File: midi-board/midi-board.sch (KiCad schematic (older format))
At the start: 22 parts, among them J1 MIDI OUT, J2 MIDI IN, J3 UART Header, U1 74LVC1G06, U2 74LVC1G17, U3 TLP185(SE

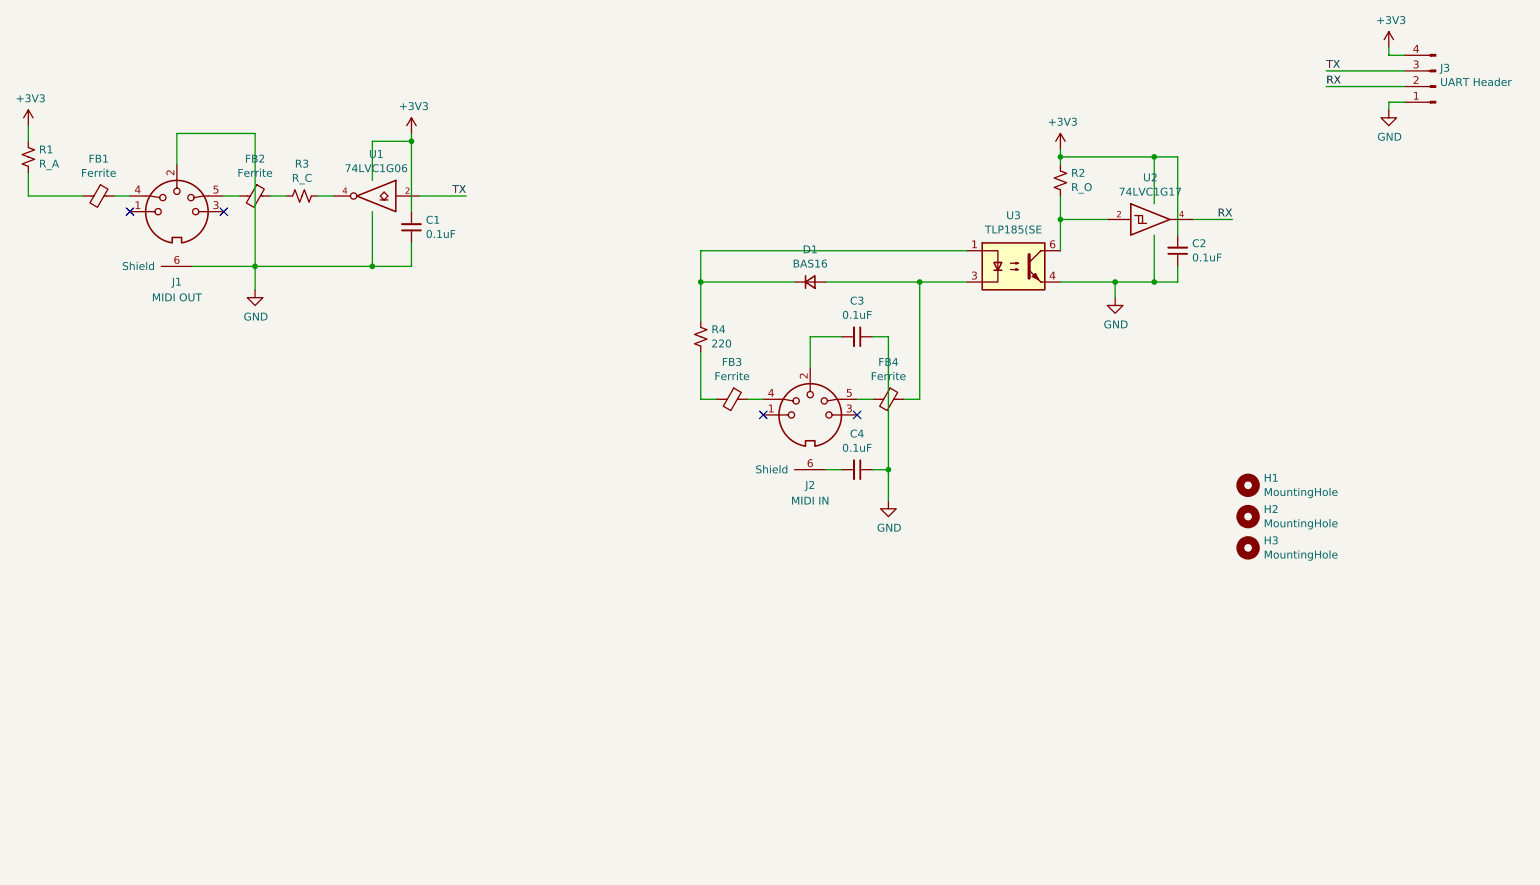
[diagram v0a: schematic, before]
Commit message: Converted MIDI board to I2C
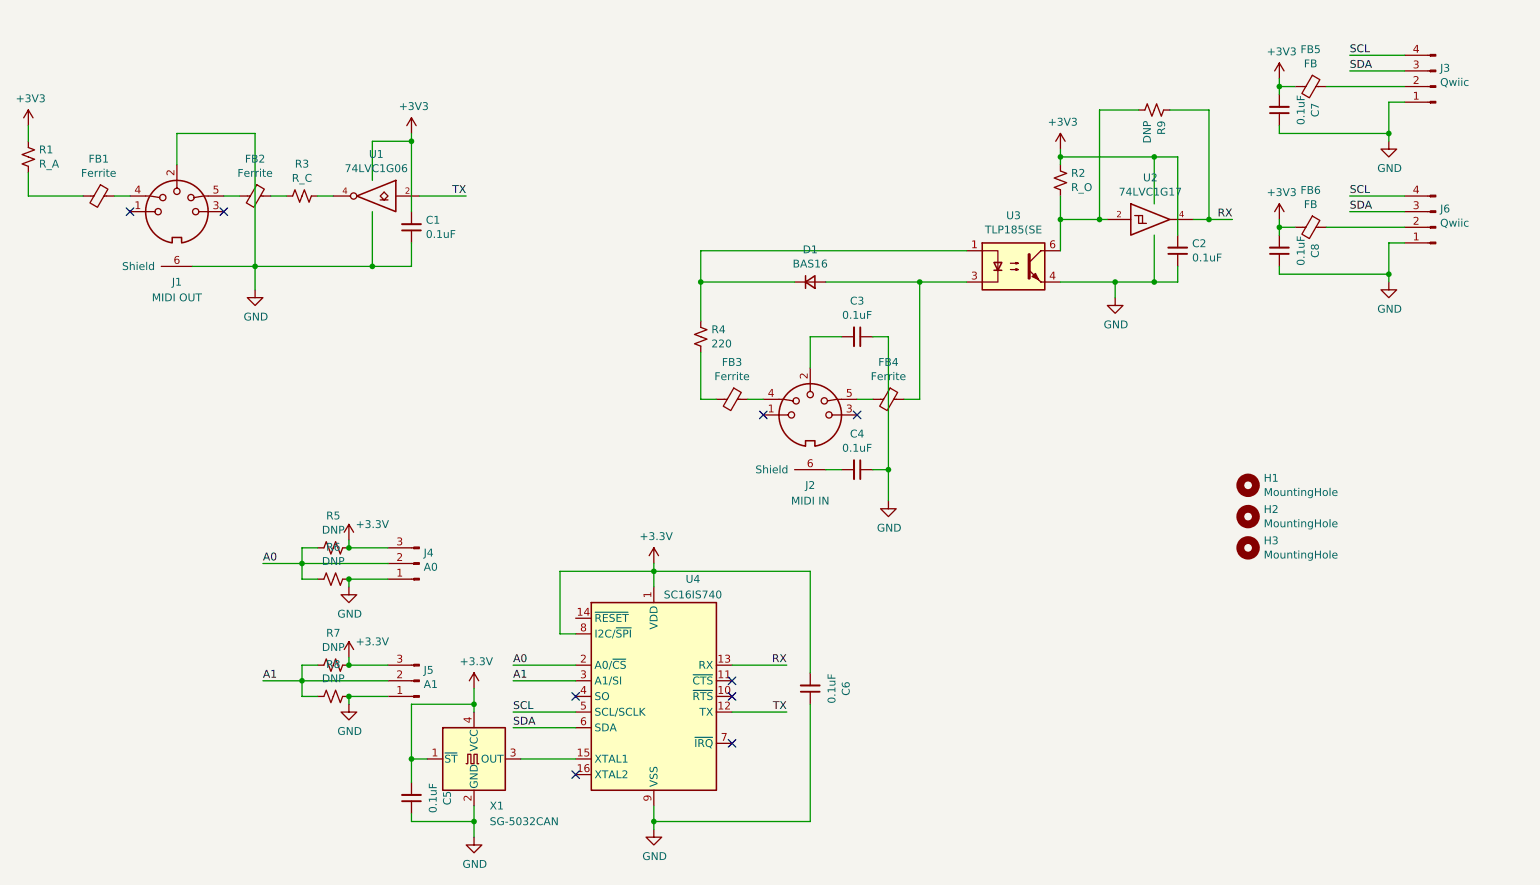
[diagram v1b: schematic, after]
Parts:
- added C5, C6, C7, C8: 0.1uF, Capacitors_SMD:C_0805_HandSoldering, symbol Device:C_Small
- added FB5, FB6: FB, Inductors_SMD:L_0805_HandSoldering, symbol Device:Ferrite_Bead_Small
- added J4: A0, Pin_Headers:Pin_Header_Straight_1x03_Pitch2.54mm, symbol Connector:Conn_01x03_Male
- added J5: A1, Pin_Headers:Pin_Header_Straight_1x03_Pitch2.54mm, symbol Connector:Conn_01x03_Male
- added J6: Qwiic, Connectors_JST:JST_SH_SM04B-SRSS-TB_04x1.00mm_Angled, symbol Connector:Conn_01x04_Male
- added R5, R6, R7, R8, R9: DNP, Resistors_SMD:R_0805_HandSoldering, symbol Device:R_Small_US
- added U4: SC16IS740, Housings_SSOP:TSSOP-16_4.4x5mm_Pitch0.65mm, symbol Interface_UART:SC16IS740
- added X1: SG-5032CAN, Oscillators:Oscillator_SMD_SeikoEpson_SG8002CE-4pin_3.2x2.5mm_HandSoldering, symbol Oscillator:SG-5032CAN
- J3: value UART Header -> Qwiic; footprint Pin_Headers:Pin_Header_Angled_1x04_Pitch2.54mm -> Connectors_JST:JST_SH_SM04B-SRSS-TB_04x1.00mm_Angled
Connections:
- net +3V3: now also C5.2, C6.2, C7.2, C8.2, FB5.2, FB6.2, J4.3 (Pin_3), J5.3 (Pin_3), R5.1, R7.1, U4.1 (VDD), U4.8 (I2C/~SPI), X1.1 (~ST), X1.4 (VCC); no longer J3.4 (Pin_4)
- net GND: now also C5.1, C6.1, C7.1, C8.1, J4.1 (Pin_1), J5.1 (Pin_1), J6.1 (Pin_1), R6.1, R8.1, U4.9 (VSS), X1.2 (GND)
- net RX: now also R9.1, U4.13 (RX); no longer J3.2 (Pin_2)
- net TX: now also U4.12 (TX); no longer J3.3 (Pin_3)
- net at R2.2, U2.2, U3.6: now also R9.2
- new net: FB5.1, J3.2 (Pin_2)
- new net: U4.15 (XTAL1), X1.3 (OUT)
- new net: FB6.1, J6.2 (Pin_2)
- new net A0: J4.2 (Pin_2), R5.2, R6.2, U4.2 (A0/~CS)
- new net A1: J5.2 (Pin_2), R7.2, R8.2, U4.3 (A1/SI)
- new net SCL: J3.4 (Pin_4), J6.4 (Pin_4), U4.5 (SCL/SCLK)
- new net SDA: J3.3 (Pin_3), J6.3 (Pin_3), U4.6 (SDA)
- no-connect marks 4 -> 9

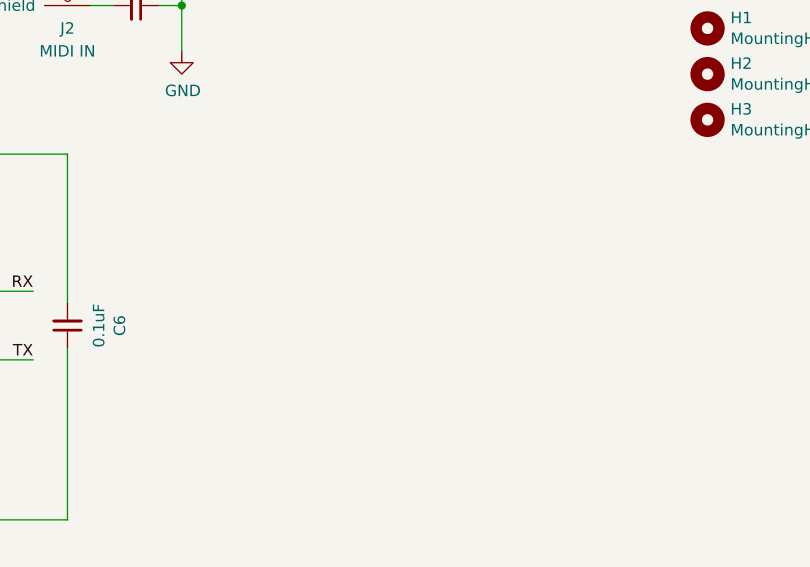
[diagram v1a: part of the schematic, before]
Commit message: Include a debug header for the TX/RX lines in their TTL state.
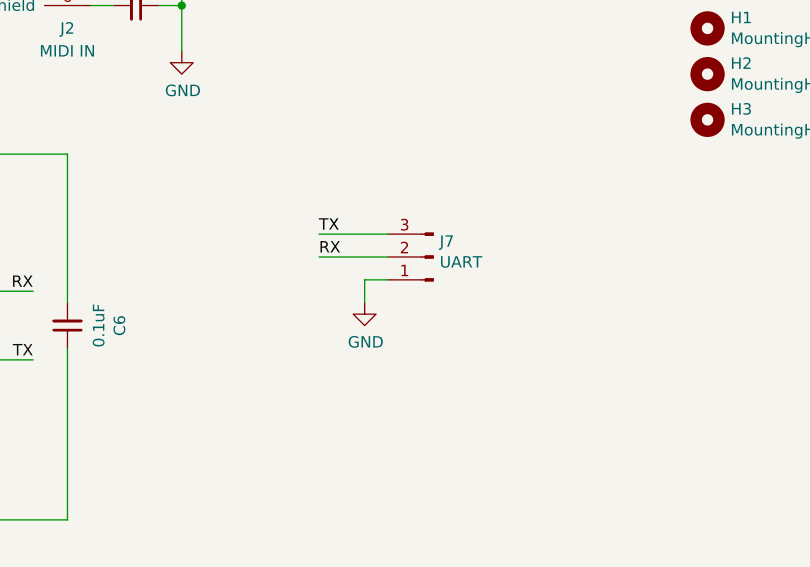
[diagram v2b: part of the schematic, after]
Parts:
- added J7: UART, Pin_Headers:Pin_Header_Straight_1x03_Pitch2.54mm, symbol Connector:Conn_01x03_Male
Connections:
- net GND: now also J7.1 (Pin_1)
- net RX: now also J7.2 (Pin_2)
- net TX: now also J7.3 (Pin_3)
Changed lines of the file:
@@
 Wire Wire Line
 	8750 2100 8900 2100
+$Comp
+L Connector:Conn_01x03_Male J7
+U 1 1 5FFC58E3
+P 7800 4800
+F 0 "J7" H 7772 4732 50  0000 R CNN
+F 1 "UART" H 7772 4823 50  0000 R CNN
+F 2 "Pin_Headers:Pin_Header_Straight_1x03_Pitch2.54mm" H 7800 4800 50  0001 C CNN
+F 3 "~" H 7800 4800 50  0001 C CNN
+	1    7800 4800
+	-1   0    0    1
+$EndComp
+Wire Wire Line
+	7600 4900 7500 4900
+Wire Wire Line
+	7500 4900 7500 5000
+$Comp
+L power:GND #PWR0119
+U 1 1 5FFCB599
+P 7500 5000
+F 0 "#PWR0119" H 7500 4750 50  0001 C CNN
+F 1 "GND" H 7505 4827 50  0000 C CNN
+F 2 "" H 7500 5000 50  0001 C CNN
+F 3 "" H 7500 5000 50  0001 C CNN
+	1    7500 5000
+	1    0    0    -1
+$EndComp
+Wire Wire Line
+	7600 4800 7300 4800
+Wire Wire Line
+	7600 4700 7300 4700
+Text Label 7300 4700 0    50   ~ 0
+TX
+Text Label 7300 4800 0    50   ~ 0
+RX
 $EndSCHEMATC

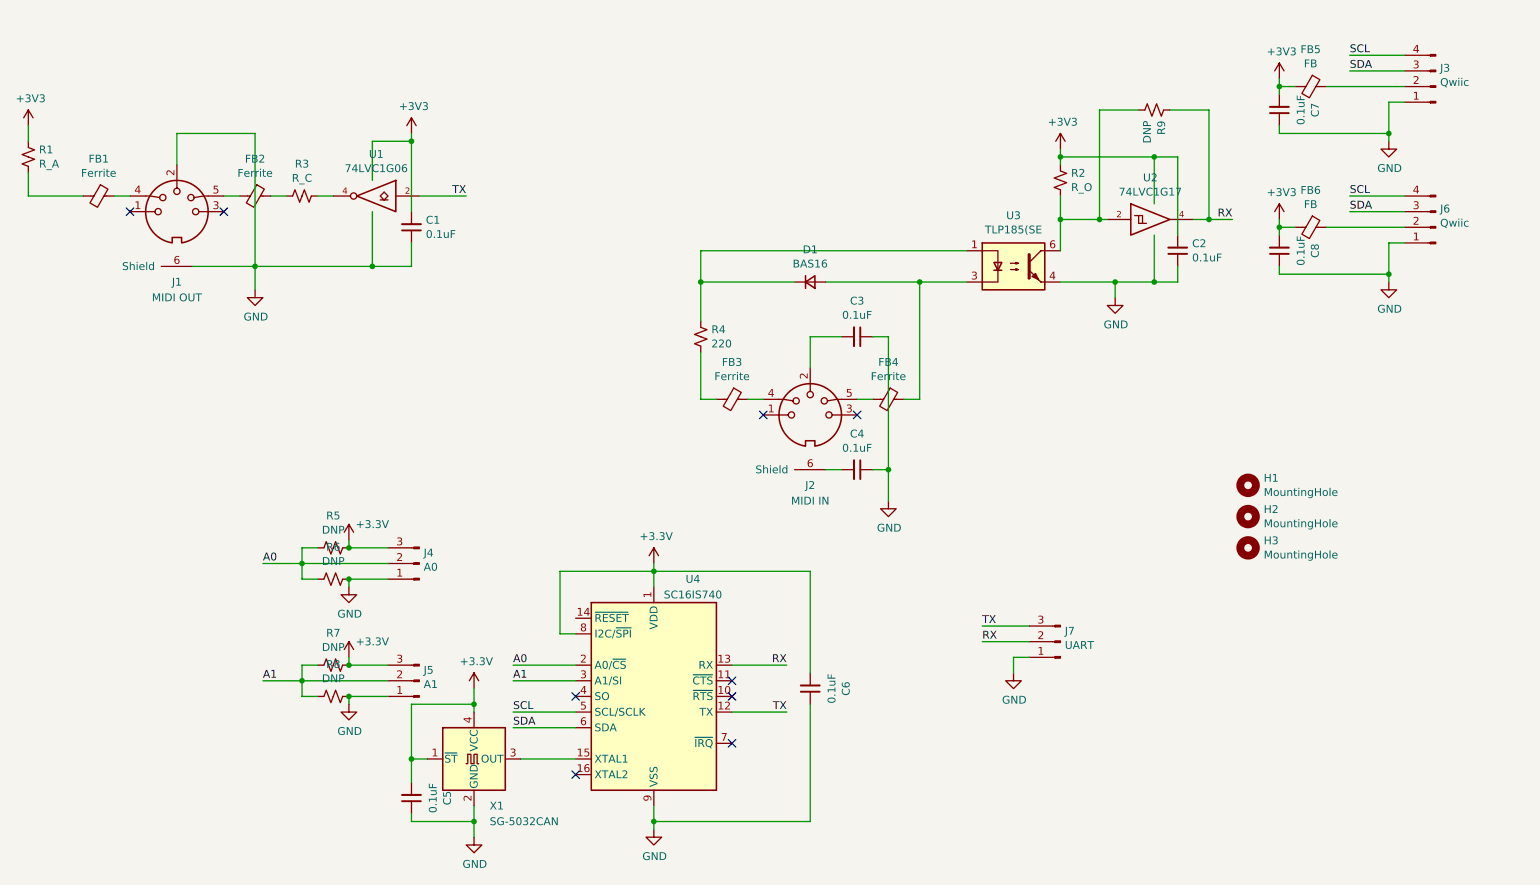
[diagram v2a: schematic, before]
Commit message: Remove unnecessary buffer, finish up reset line(s).
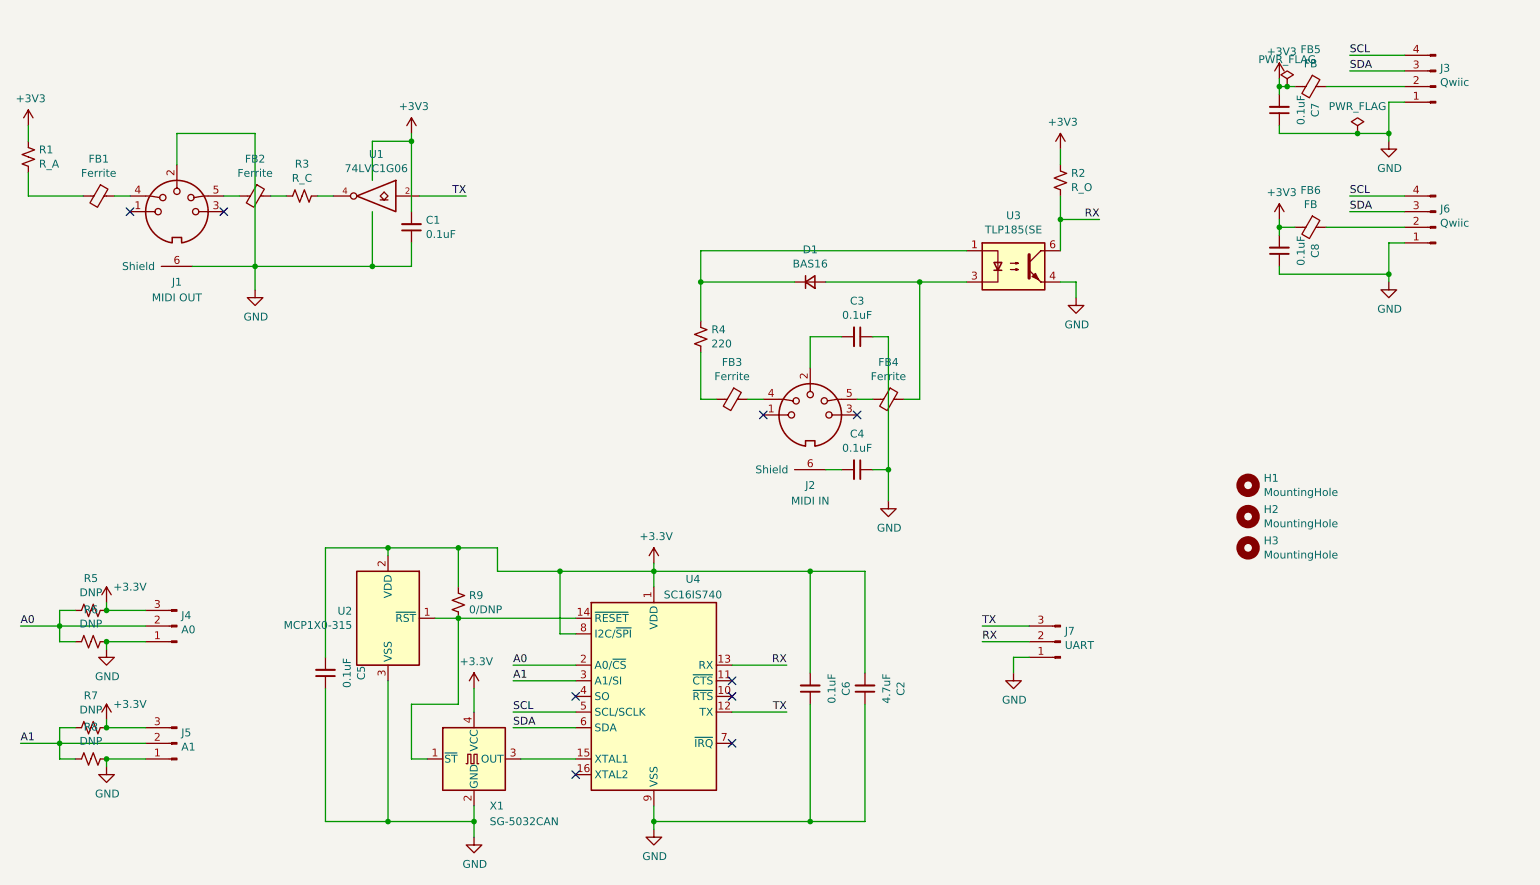
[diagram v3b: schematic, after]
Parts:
- removed U2: 74LVC1G17, TO_SOT_Packages_SMD:SOT-353_SC-70-5_Handsoldering, symbol 74xGxx:74LVC1G17
- added U2: MCP1X0-315, TO_SOT_Packages_SMD:SOT-23, symbol Power_Supervisor:MCP120-xxxxTT
- C2: value 0.1uF -> 4.7uF
- R9: value DNP -> 0/DNP
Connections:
- net +3V3: now also R9.2, U2.2 (VDD); no longer X1.1 (~ST)
- net GND: now also U2.3 (VSS)
- net RX: now also R2.2, U3.6; no longer R9.1
- net at U4.14 (~RESET): now also R9.1, X1.1 (~ST), U2.1 (~RST)
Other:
- moved on the sheet: C5, J4, J5, R5, R6, R7, R8
